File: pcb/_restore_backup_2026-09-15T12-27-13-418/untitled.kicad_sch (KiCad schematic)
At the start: 1 part, among them U2 TPS54325PWP

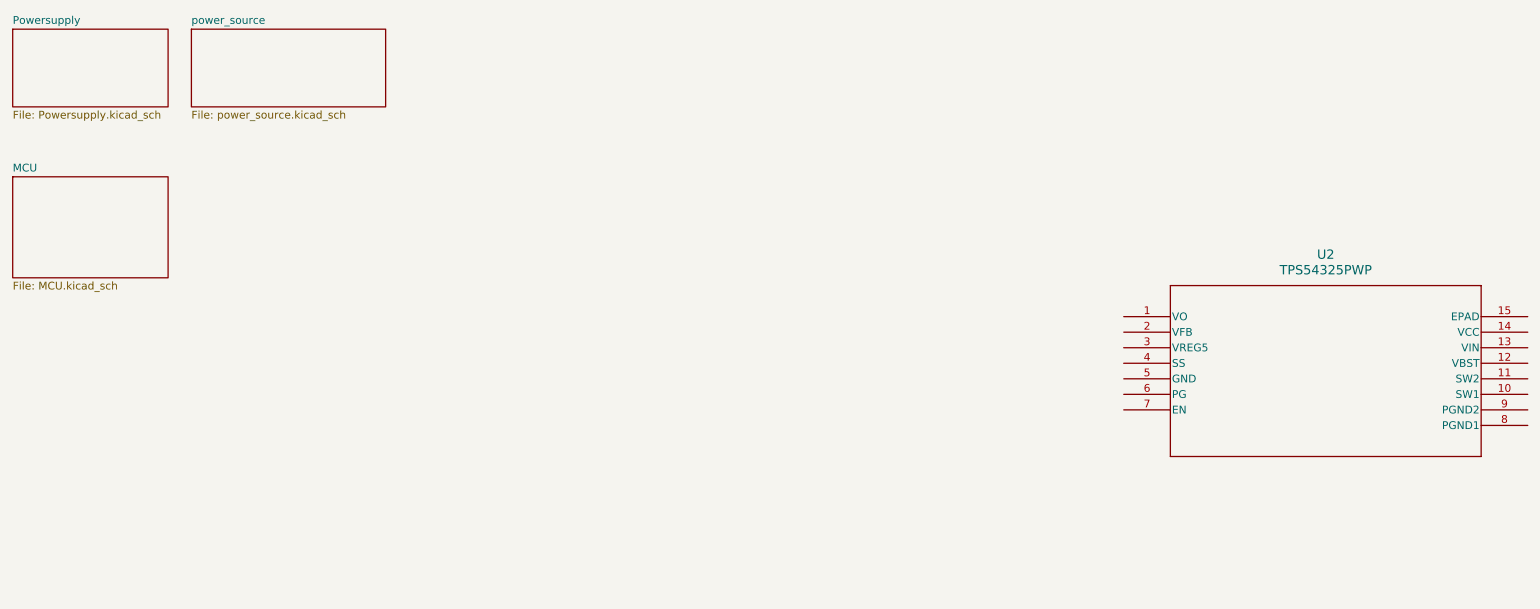
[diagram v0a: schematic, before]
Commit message: add microsd
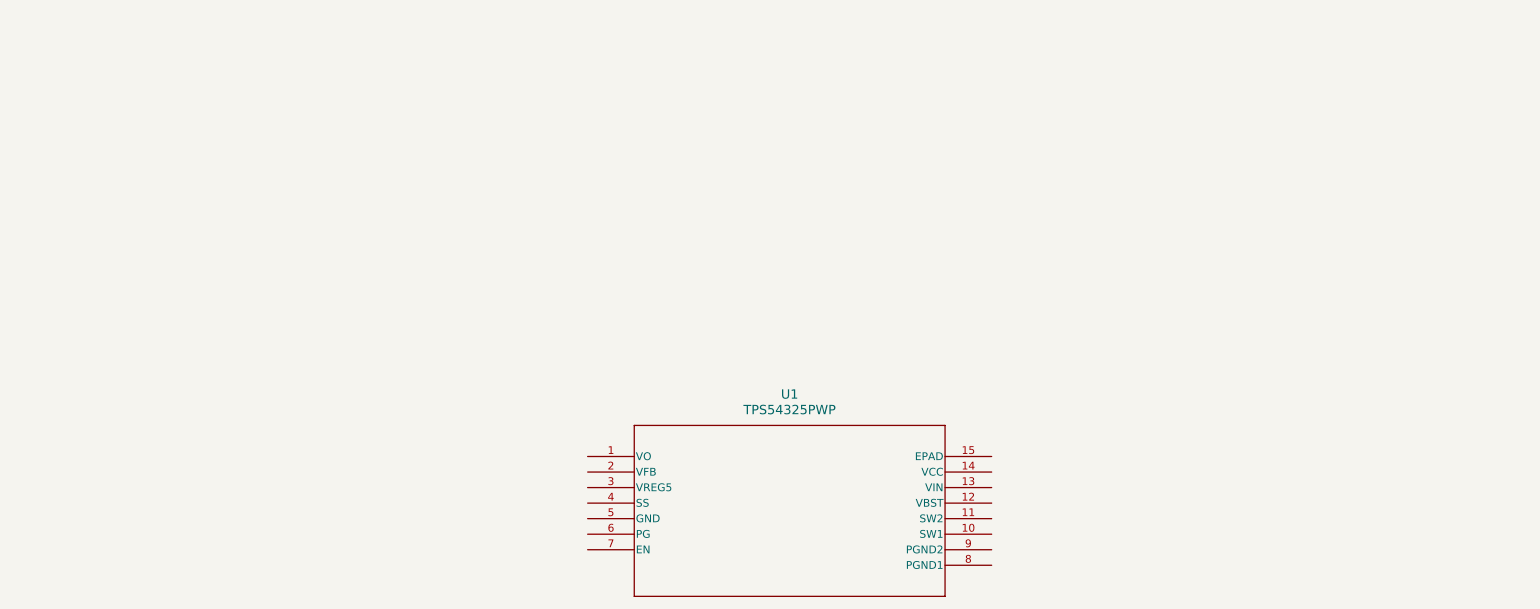
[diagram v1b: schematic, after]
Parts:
- removed U2: TPS54325PWP, PWP14_2P31X2P46, symbol TPS54325:TPS54325PWP
- added U1: TPS54325PWP, PWP14_2P31X2P46, symbol TPS54325:TPS54325PWP
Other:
- removed sheet MCU
- removed sheet Powersupply
- removed sheet power_source
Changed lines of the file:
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@@
 	(symbol
 		(lib_id "TPS54325:TPS54325PWP")
-		(at 193.04 67.31 0)
+		(at 105.41 90.17 0)
 		(unit 1)
 		(body_style 1)
@@
 		(dnp no)
 		(fields_autoplaced yes)
-		(property "Reference" "U2"
-			(at 240.03 74.93 0)
+		(property "Reference" "U1"
+			(at 152.4 97.79 0)
 			(show_name no)
 			(do_not_autoplace no)
@@
 		)
 		(property "Value" "TPS54325PWP"
-			(at 240.03 77.47 0)
+			(at 152.4 100.33 0)
 			(show_name no)
 			(do_not_autoplace no)
@@
 		)
 		(property "Footprint" "PWP14_2P31X2P46"
-			(at 207.01 85.09 0)
+			(at 119.38 107.95 0)
 			(hide yes)
 			(show_name no)
@@
 		)
 		(property "Datasheet" "https://www.ti.com/lit/gpn/tps54325"
-			(at 193.04 67.31 0)
+			(at 105.41 90.17 0)
 			(hide yes)
 			(show_name no)
@@
 		)
 		(property "Description" ""
-			(at 193.04 67.31 0)
+			(at 105.41 90.17 0)
 			(hide yes)
 			(show_name no)
@@
 		(instances
 			(project "tdt4295"
-				(path "/603dd496-f9c4-4a31-9104-19eec41ebc98"
-					(reference "U2")
+				(path "/603dd496-f9c4-4a31-9104-19eec41ebc98/9989e047-3a4b-42fb-8136-c8ce73468c70"
+					(reference "U1")
 					(unit 1)
 				)
@@
 		)
 	)
-	(sheet
-		(at 54.61 38.1)
-		(size 31.75 12.7)
-		(exclude_from_sim no)
-		(in_bom yes)
-		(on_board yes)
-		(dnp no)
-		(fields_autoplaced yes)
-		(stroke
-			(width 0.1524)
-			(type solid)
-		)
-		(fill
-			(color 0 0 0 0)
-		)
-		(property "Sheetname" "power_source"
-			(at 54.61 37.3884 0)
-			(show_name no)
-			(do_not_autoplace no)
-			(effects
-				(font
-					(size 1.27 1.27)
-				)
-				(justify left bottom)
-			)
-		)
-		(property "Sheetfile" "power_source.kicad_sch"
-			(at 54.61 51.3846 0)
-			(show_name no)
-			(do_not_autoplace no)
-			(effects
-				(font
-					(size 1.27 1.27)
-				)
-				(justify left top)
-			)
-		)
-		(instances
-			(project "tdt4295"
-				(path "/603dd496-f9c4-4a31-9104-19eec41ebc98"
-					(page "7")
-				)
-			)
-		)
-	)
-	(sheet
-		(at 25.4 62.23)
-		(size 25.4 16.51)
-		(exclude_from_sim no)
-		(in_bom yes)
-		(on_board yes)
-		(dnp no)
-		(fields_autoplaced yes)
-		(stroke
-			(width 0.1524)
-			(type solid)
-		)
-		(fill
-			(color 0 0 0 0)
-		)
-		(property "Sheetname" "MCU"
-			(at 25.4 61.5184 0)
-			(show_name no)
-			(do_not_autoplace no)
-			(effects
-				(font
-					(size 1.27 1.27)
-				)
-				(justify left bottom)
-			)
-		)
-		(property "Sheetfile" "MCU.kicad_sch"
-			(at 25.4 79.3246 0)
-			(show_name no)
-			(do_not_autoplace no)
-			(effects
-				(font
-					(size 1.27 1.27)
-				)
-				(justify left top)
-			)
-		)
-		(instances
-			(project "tdt4295"
-				(path "/603dd496-f9c4-4a31-9104-19eec41ebc98"
-					(page "5")
-				)
-			)
-		)
-	)
-	(sheet
-		(at 25.4 38.1)
-		(size 25.4 12.7)
-		(exclude_from_sim no)
-		(in_bom yes)
-		(on_board yes)
-		(dnp no)
-		(fields_autoplaced yes)
-		(stroke
-			(width 0.1524)
-			(type solid)
-		)
-		(fill
-			(color 0 0 0 0)
-		)
-		(property "Sheetname" "Powersupply"
-			(at 25.4 37.3884 0)
-			(show_name no)
-			(do_not_autoplace no)
-			(effects
-				(font
-					(size 1.27 1.27)
-				)
-				(justify left bottom)
-			)
-		)
-		(property "Sheetfile" "Powersupply.kicad_sch"
-			(at 25.4 51.3846 0)
-			(show_name no)
-			(do_not_autoplace no)
-			(effects
-				(font
-					(size 1.27 1.27)
-				)
-				(justify left top)
-			)
-		)
-		(instances
-			(project "tdt4295"
-				(path "/603dd496-f9c4-4a31-9104-19eec41ebc98"
-					(page "4")
-				)
-			)
-		)
-	)
-	(sheet_instances
-		(path "/"
-			(page "1")
-		)
-	)
-	(embedded_fonts no)
 )
